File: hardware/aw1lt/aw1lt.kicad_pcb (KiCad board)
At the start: 2 copper layers, 30 x 22 mm, 27 parts, among them J1 ISP_FTDI, Q1 Q_NPN_CBE, SW1 SW_Push, SW2 SW_Push, SW3 SW_Push, U1 DS3231MZ, U2 ATMEGA328P-AU

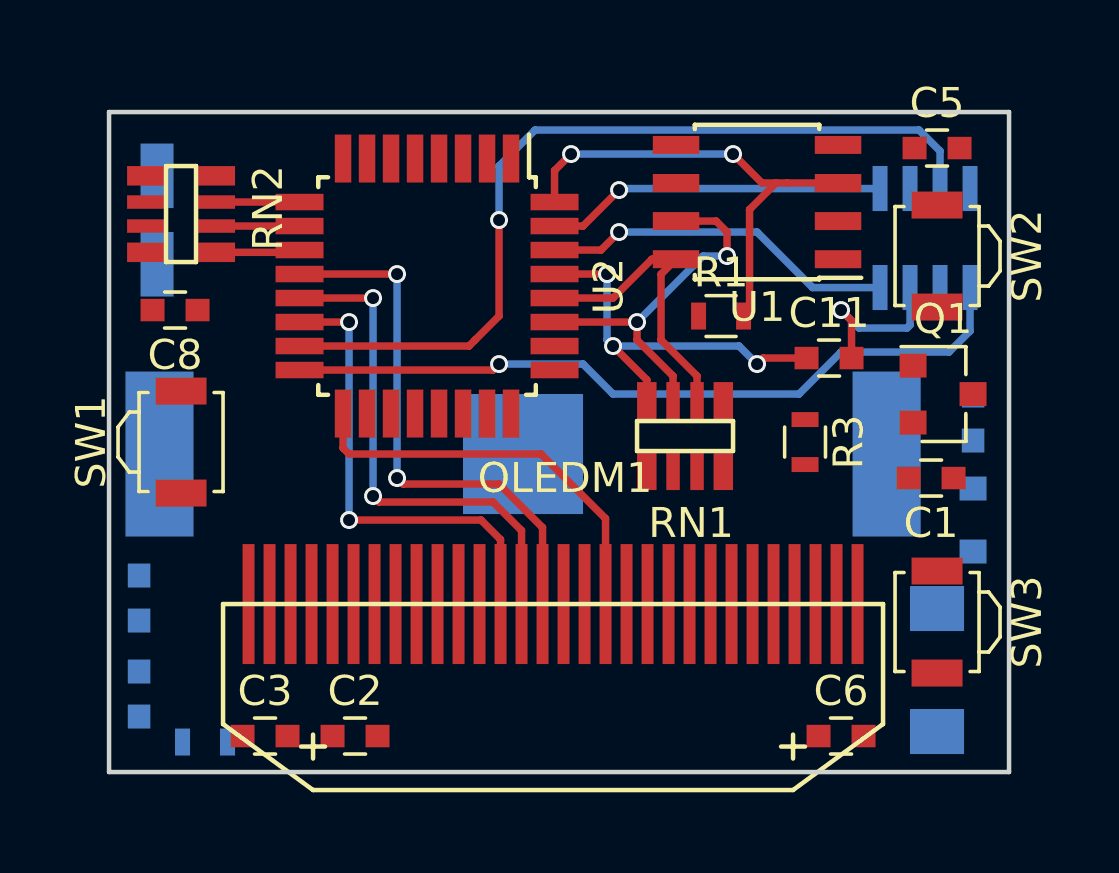
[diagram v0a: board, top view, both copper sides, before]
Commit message: modified a bit of the layout, rotated some parts, got rid of a resistor network in favor of individual resistors for more flexibility
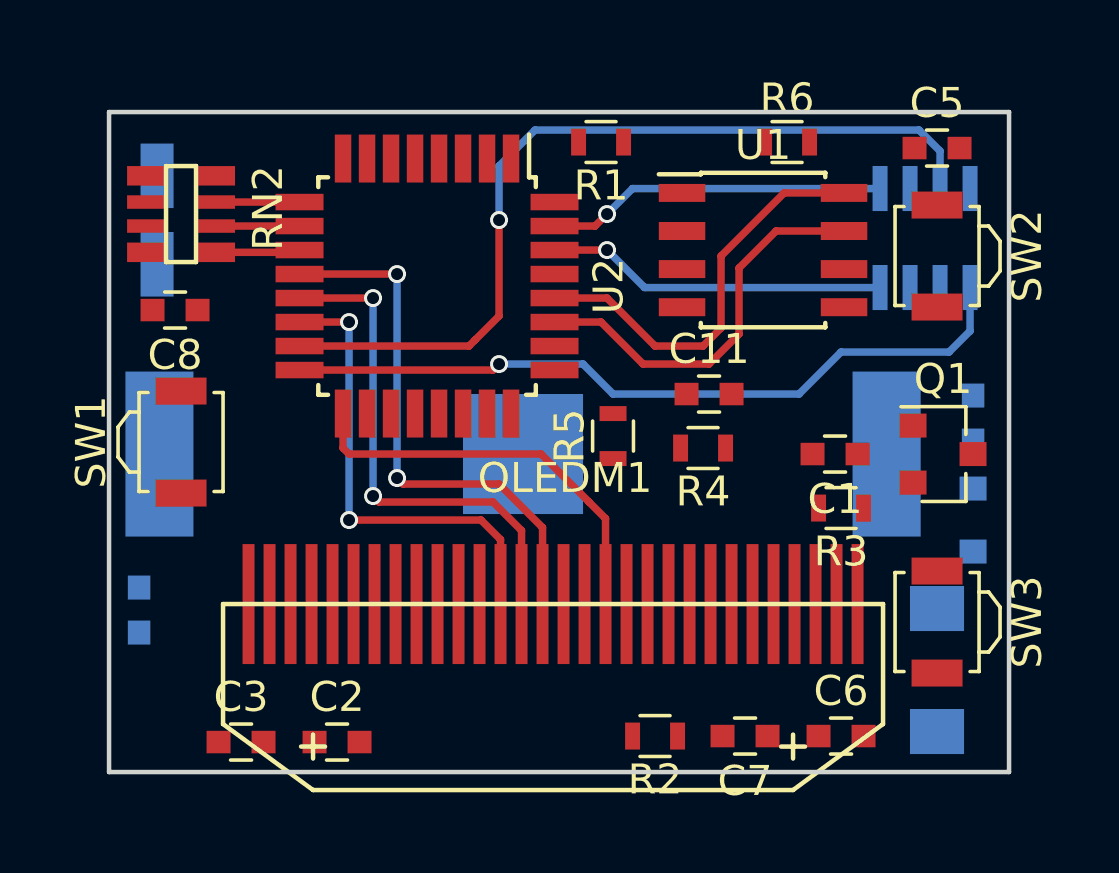
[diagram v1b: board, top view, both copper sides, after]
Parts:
- removed RN1: 10K, aw-1:EXB38V
- added R4: 10K, Resistors_SMD:R_0603, F.Cu at (144.8, 136.2)
- added R5: 10K, Resistors_SMD:R_0603, F.Cu at (141.8, 135.8)
- added R6: 10K, Resistors_SMD:R_0603, F.Cu at (147.6, 126.0)
- C7, R2: moved to F.Cu
- moved C7 20.2 mm to (146.2, 145.8), turned to 180 degrees
- moved R2 15.0 mm to (143.2, 145.8)
- moved R1 7.05 mm to (141.4, 126.0), turned to 180 degrees
- moved C11 4.18 mm to (145.0, 134.4)
- moved C1 3.30 mm to (149.2, 136.4)
- moved R3 2.51 mm to (149.4, 138.2), turned to 180 degrees
- moved Q1 2.00 mm to (152.8, 136.4)
- moved U1 1.61 mm to (146.8, 129.6), turned to 0 degrees
- moved C3 0.82 mm to (129.4, 146.0)
- moved C2 0.63 mm to (132.6, 146.0)
- moved C10 0.40 mm to (126.0, 141.6)
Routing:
- net INT0: track 16.0 -> 0.05 mm, vias 2 -> 0
- net Net-(C11-Pad1): track 13.1 -> 0.00 mm, vias 3 -> 0
- net DTR: track 5.58 -> 0.00 mm, vias 1 -> 0
- net SCL: track 10.0 -> 13.8 mm
- net SDA: track 12.5 -> 13.4 mm, vias 2 -> 0

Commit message: making progress on routing
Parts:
- moved R1 1.00 mm to (142.4, 126.0)
- moved C5 0.89 mm to (153.4, 125.8)
- moved C4 0.63 mm to (154.0, 134.6)
- moved R5 0.63 mm to (142.4, 136.0)
- moved R4 0.20 mm to (145.0, 136.2)
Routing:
- net PB1: track 2.80 -> 27.8 mm, vias 0 -> 2
- net SCK: track 13.7 -> 35.6 mm, vias 0 -> 3
- net PB0: track 2.80 -> 19.9 mm, vias 0 -> 2
- net Net-(C8-Pad1): track 0.00 -> 13.7 mm, vias 0 -> 2
- net SPKR: track 0.00 -> 11.6 mm
- net DTR: track 0.00 -> 10.6 mm, vias 0 -> 1
- net INT0: track 0.05 -> 9.97 mm
- net Net-(C11-Pad1): track 0.00 -> 9.38 mm, vias 0 -> 2
- net Net-(BZ1-Pad2): track 0.00 -> 8.34 mm, vias 0 -> 1
- net Net-(OLEDM1-Pad26): track 0.00 -> 7.01 mm
- net Net-(C3-Pad1): track 0.00 -> 5.30 mm
- net Net-(C3-Pad2): track 0.00 -> 4.97 mm
- net Net-(C2-Pad2): track 0.00 -> 4.97 mm
- net Net-(C7-Pad1): track 0.00 -> 4.77 mm
- net Net-(C2-Pad1): track 0.00 -> 4.64 mm
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
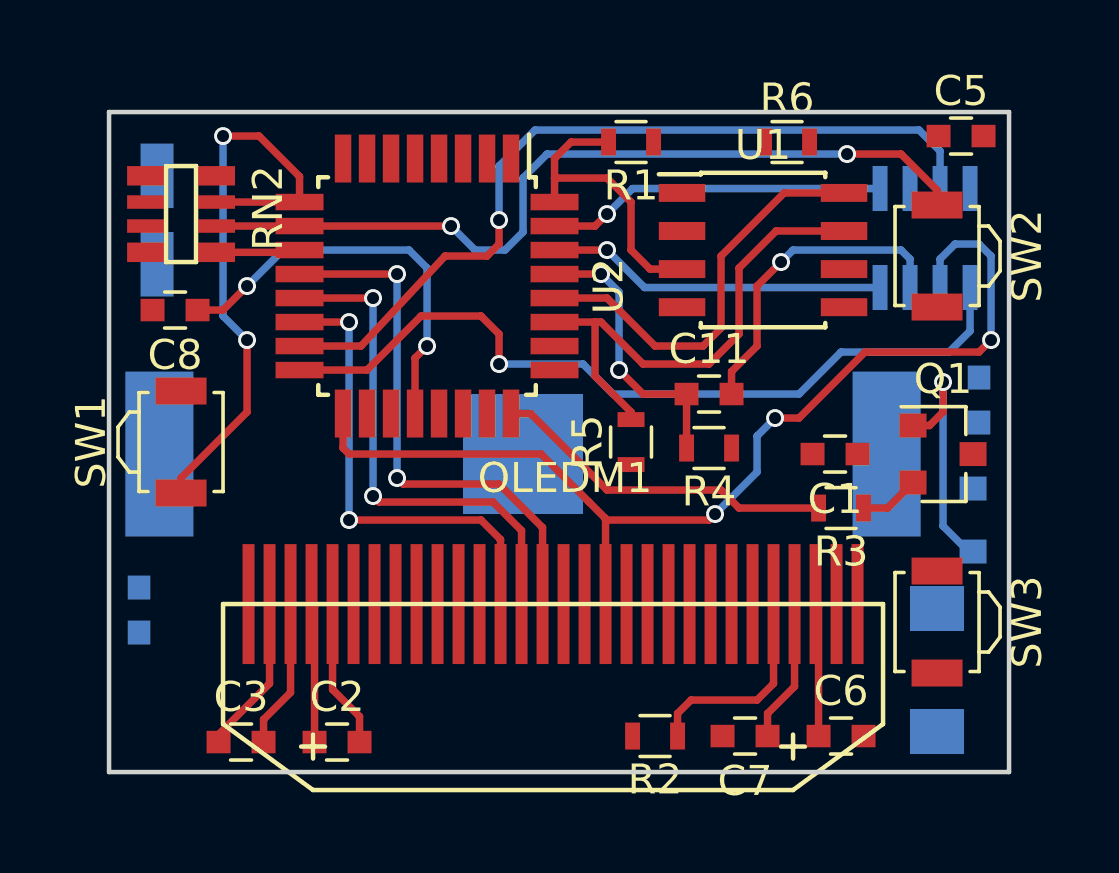
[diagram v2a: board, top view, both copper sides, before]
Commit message: have all the pins routed, now need to connect the grounds and power with copper pours
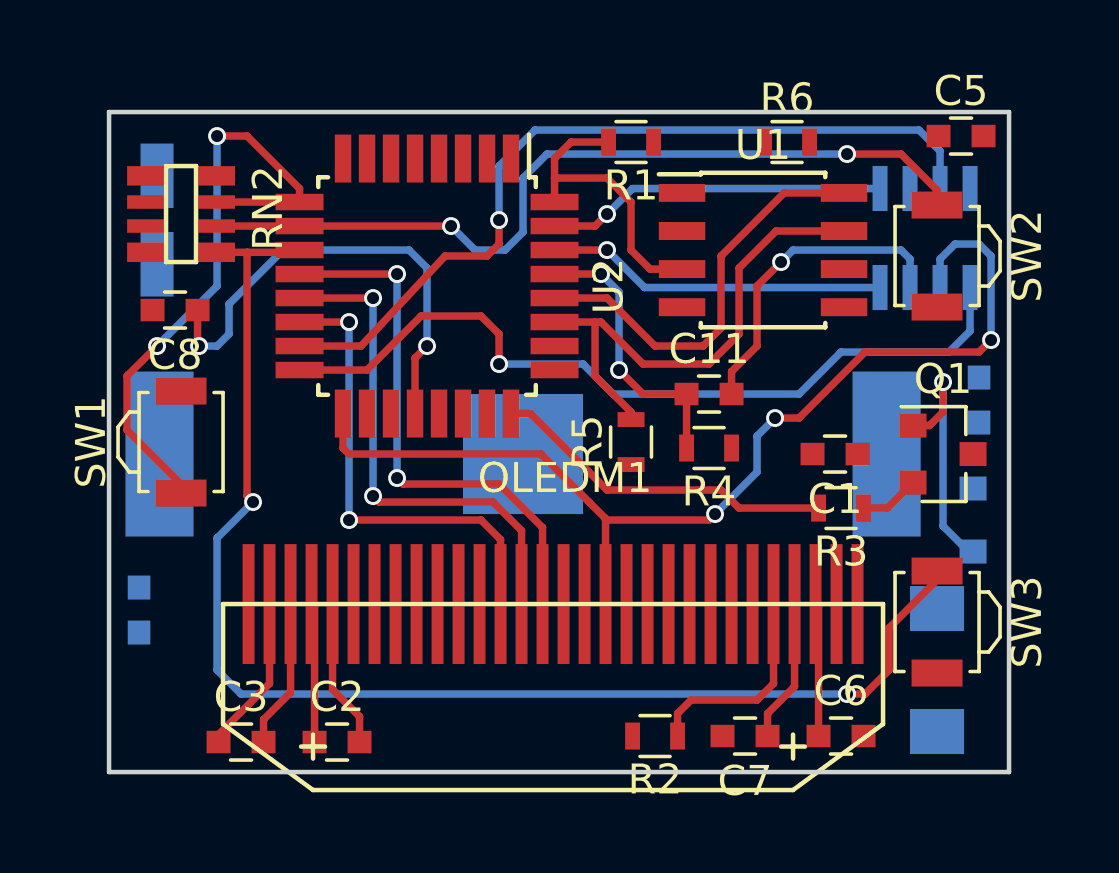
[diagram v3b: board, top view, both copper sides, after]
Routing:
- net PB2: track 2.94 -> 44.5 mm, vias 0 -> 2
- net Net-(C8-Pad1): track 13.7 -> 16.0 mm
- net PB0: track 19.9 -> 20.6 mm
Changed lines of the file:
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@@
   (general
     (links 93)
-    (no_connects 60)
+    (no_connects 59)
     (area 124.924999 124.924999 155.075001 147.075001)
     (thickness 1.6)
     (drawings 4)
-    (tracks 197)
+    (tracks 216)
     (zones 0)
     (modules 29)
@@
   (segment (start 147.85 144.15) (end 147.85 141.4) (width 0.25) (layer F.Cu) (net 8))
   (segment (start 146.95 145.05) (end 147.85 144.15) (width 0.25) (layer F.Cu) (net 8))
-  (segment (start 127.95 131.6) (end 128.8 131.6) (width 0.25) (layer F.Cu) (net 9) (status 400000))
+  (segment (start 127.95 131.6) (end 127.95 132.75) (width 0.25) (layer F.Cu) (net 9) (status 400000))
+  (segment (start 129.6 130.8) (end 130.8 129.6) (width 0.25) (layer B.Cu) (net 9))
+  (segment (start 130.8 129.6) (end 135 129.6) (width 0.25) (layer B.Cu) (net 9))
+  (segment (start 135 129.6) (end 135.6 130.2) (width 0.25) (layer B.Cu) (net 9))
+  (segment (start 135.6 130.2) (end 135.6 132.8) (width 0.25) (layer B.Cu) (net 9))
+  (via (at 135.6 132.8) (size 0.6) (drill 0.4) (layers F.Cu B.Cu) (net 9))
+  (segment (start 135.6 132.8) (end 135.2 133.2) (width 0.25) (layer F.Cu) (net 9))
   (segment (start 135.2 133.2) (end 135.2 135.05) (width 0.25) (layer F.Cu) (net 9) (status 800000))
-  (segment (start 135.6 132.8) (end 135.2 133.2) (width 0.25) (layer F.Cu) (net 9))
-  (via (at 135.6 132.8) (size 0.6) (drill 0.4) (layers F.Cu B.Cu) (net 9))
-  (segment (start 135.6 130.2) (end 135.6 132.8) (width 0.25) (layer B.Cu) (net 9))
-  (segment (start 135 129.6) (end 135.6 130.2) (width 0.25) (layer B.Cu) (net 9))
-  (segment (start 130.8 129.6) (end 135 129.6) (width 0.25) (layer B.Cu) (net 9))
-  (segment (start 129.6 130.8) (end 130.8 129.6) (width 0.25) (layer B.Cu) (net 9))
-  (via (at 129.6 130.8) (size 0.6) (drill 0.4) (layers F.Cu B.Cu) (net 9))
-  (segment (start 128.8 131.6) (end 129.6 130.8) (width 0.25) (layer F.Cu) (net 9))
+  (segment (start 129 131.4) (end 129.6 130.8) (width 0.25) (layer B.Cu) (net 9))
+  (segment (start 129 132.4) (end 129 131.4) (width 0.25) (layer B.Cu) (net 9))
+  (segment (start 128.6 132.8) (end 129 132.4) (width 0.25) (layer B.Cu) (net 9))
+  (segment (start 128 132.8) (end 128.6 132.8) (width 0.25) (layer B.Cu) (net 9))
+  (via (at 128 132.8) (size 0.6) (drill 0.4) (layers F.Cu B.Cu) (net 9))
+  (segment (start 127.95 132.75) (end 128 132.8) (width 0.25) (layer F.Cu) (net 9))
   (segment (start 144.25 134.4) (end 142.8 134.4) (width 0.25) (layer F.Cu) (net 10))
   (segment (start 141.4 130.4) (end 139.85 130.4) (width 0.25) (layer F.Cu) (net 10))
@@
   (segment (start 145.4 129.8) (end 145.4 132.2) (width 0.25) (layer F.Cu) (net 25))
   (segment (start 147.505 127.695) (end 145.4 129.8) (width 0.25) (layer F.Cu) (net 25))
-  (segment (start 127.4 137.7) (end 127.4 137.2) (width 0.25) (layer F.Cu) (net 26) (status 400000))
-  (segment (start 131.35 127.15) (end 131.35 128) (width 0.25) (layer F.Cu) (net 26) (status 800000))
-  (segment (start 130 125.8) (end 131.35 127.15) (width 0.25) (layer F.Cu) (net 26))
-  (segment (start 128.8 125.8) (end 130 125.8) (width 0.25) (layer F.Cu) (net 26))
-  (via (at 128.8 125.8) (size 0.6) (drill 0.4) (layers F.Cu B.Cu) (net 26))
-  (segment (start 128.8 131.8) (end 128.8 125.8) (width 0.25) (layer B.Cu) (net 26))
-  (segment (start 129.6 132.6) (end 128.8 131.8) (width 0.25) (layer B.Cu) (net 26))
-  (via (at 129.6 132.6) (size 0.6) (drill 0.4) (layers F.Cu B.Cu) (net 26))
-  (segment (start 129.6 135) (end 129.6 132.6) (width 0.25) (layer F.Cu) (net 26))
-  (segment (start 127.4 137.2) (end 129.6 135) (width 0.25) (layer F.Cu) (net 26))
+  (segment (start 127.4 137.7) (end 127.4 137.4) (width 0.25) (layer F.Cu) (net 26) (status C00000))
+  (segment (start 127.4 137.4) (end 125.6 135.6) (width 0.25) (layer F.Cu) (net 26) (status 400000))
+  (segment (start 125.6 135.6) (end 125.6 133.8) (width 0.25) (layer F.Cu) (net 26))
+  (segment (start 125.6 133.8) (end 126.6 132.8) (width 0.25) (layer F.Cu) (net 26))
+  (via (at 126.6 132.8) (size 0.6) (drill 0.4) (layers F.Cu B.Cu) (net 26))
+  (segment (start 126.6 132.8) (end 128.6 130.8) (width 0.25) (layer B.Cu) (net 26))
+  (segment (start 128.6 130.8) (end 128.6 125.8) (width 0.25) (layer B.Cu) (net 26))
+  (via (at 128.6 125.8) (size 0.6) (drill 0.4) (layers F.Cu B.Cu) (net 26))
+  (segment (start 128.6 125.8) (end 129.6 125.8) (width 0.25) (layer F.Cu) (net 26))
+  (segment (start 129.6 125.8) (end 131.35 127.55) (width 0.25) (layer F.Cu) (net 26))
+  (segment (start 131.35 127.55) (end 131.35 128) (width 0.25) (layer F.Cu) (net 26) (status 800000))
   (segment (start 128.55 128) (end 131.35 128) (width 0.25) (layer F.Cu) (net 26))
   (segment (start 152.6 128.1) (end 152.6 127.6) (width 0.25) (layer F.Cu) (net 27))
@@
   (segment (start 152.6 127.6) (end 151.4 126.4) (width 0.25) (layer F.Cu) (net 27))
   (segment (start 128.55 128.8) (end 131.35 128.8) (width 0.25) (layer F.Cu) (net 27))
-  (segment (start 128.55 129.675) (end 131.275 129.675) (width 0.25) (layer F.Cu) (net 28))
+  (segment (start 152.6 140.3) (end 152.6 140.6) (width 0.25) (layer F.Cu) (net 28) (status C00000))
+  (segment (start 152.6 140.6) (end 151 142.2) (width 0.25) (layer F.Cu) (net 28) (status 400000))
+  (segment (start 151 142.2) (end 151 143.6) (width 0.25) (layer F.Cu) (net 28))
+  (segment (start 151 143.6) (end 150.2 144.4) (width 0.25) (layer F.Cu) (net 28))
+  (segment (start 150.2 144.4) (end 149.6 144.4) (width 0.25) (layer F.Cu) (net 28))
+  (via (at 149.6 144.4) (size 0.6) (drill 0.4) (layers F.Cu B.Cu) (net 28))
+  (segment (start 149.6 144.4) (end 129.4 144.4) (width 0.25) (layer B.Cu) (net 28))
+  (segment (start 129.4 144.4) (end 128.6 143.6) (width 0.25) (layer B.Cu) (net 28))
+  (segment (start 128.6 143.6) (end 128.6 139.2) (width 0.25) (layer B.Cu) (net 28))
+  (segment (start 128.6 139.2) (end 129.8 138) (width 0.25) (layer B.Cu) (net 28))
+  (via (at 129.8 138) (size 0.6) (drill 0.4) (layers F.Cu B.Cu) (net 28))
+  (segment (start 129.8 138) (end 129.6 137.8) (width 0.25) (layer F.Cu) (net 28))
+  (segment (start 129.6 137.8) (end 129.6 129.675) (width 0.25) (layer F.Cu) (net 28))
+  (segment (start 128.55 129.675) (end 129.6 129.675) (width 0.25) (layer F.Cu) (net 28))
+  (segment (start 129.6 129.675) (end 131.275 129.675) (width 0.25) (layer F.Cu) (net 28))
   (segment (start 131.275 129.675) (end 131.35 129.6) (width 0.25) (layer F.Cu) (net 28))
   (segment (start 128.625 129.6) (end 128.55 129.675) (width 0.25) (layer F.Cu) (net 28))

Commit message: some changes
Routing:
- net GND: track 0.00 -> 44.5 mm, vias 0 -> 16
- net +3V3: track 0.00 -> 14.9 mm, vias 0 -> 7
- added copper zone on F.Cu, net +3V3
- added copper zone on B.Cu, net GND
